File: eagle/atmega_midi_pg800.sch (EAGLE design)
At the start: 19 parts, among them IC1 78L05Z, U1 6N138, U2 ATMEGA328P_PDIP, X1 MAB6H

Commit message: routed
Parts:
- removed MIDI_IN1: MIDIJACK, adafruit:MIDIJACK
- removed RESET2: LSP11, solpad:LSP11
- added C4: 100uF, rcl:CPOL-USB45181A
- added C5: 10uF, rcl:CPOL-USB45181A
- added MIDI_THRU: MIDIJACK, adafruit:MIDIJACK
- added X2: 22-23-2081, con-molex:22-23-2081
- RESET: value LSP11 -> 22-23-2021; device solpad:LSP11 -> con-molex:22-23-2021
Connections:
- new net N$10: U2.PB2(SS/OC1B), X1.1
- new net N$11: U2.PB1(OC1A), X1.5
- new net N$12: U2.PC0(ADC0), X2-7.S
- new net N$13: U2.PC1(ADC1), X2-6.S
- new net N$14: U2.PC2(ADC2), X2-5.S
- new net N$15: U2.PC3(ADC3), X2-4.S
- new net N$16: U2.PC4(ADC4/SDA), X2-3.S
- new net N$17: U2.PC5(ADC5/SCL), X2-2.S
- new net N$2: D2.A, X1.3
- new net N$6: C4.+, D2.C, IC1.VI
- new net N$9: U2.PB0(ICP), X1.6
- net +5V: now also C5.+, IC1.VO, X2-1.S
- net GND: now also C4.-, C5.-, IC1.GND, MIDI_THRUG$1.2, MIDI_THRUG$2.MT, MIDI_THRUG$3.MT, MIDI_THRUG$4.MT, MIDI_THRUG$5.MT, RESET-1.S, X1.4, X1.PE, X2-8.S; no longer MIDI_IN1G$1.2, MIDI_IN1G$2.MT, MIDI_IN1G$3.MT, MIDI_IN1G$4.MT, MIDI_IN1G$5.MT, RESET2.MP
- net N$1: now also MIDI_THRUG$1.4; no longer MIDI_IN1G$1.4
- net N$42: now also MIDI_THRUG$1.5; no longer MIDI_IN1G$1.5
- net N$43: now also RESET-2.S; no longer RESET.MP
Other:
- moved on the sheet: D2, IC1, R3, R5

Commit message: gcode
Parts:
- Q1: value (none) -> 16.000Mhz
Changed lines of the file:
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@@
 <parts>
 <part name="U2" library="SparkFun-DigitalIC" deviceset="ATMEGA328P_PDIP" device=""/>
-<part name="Q1" library="crystal" deviceset="CRYSTAL" device="HC49S"/>
+<part name="Q1" library="crystal" deviceset="CRYSTAL" device="HC49S" value="16.000Mhz"/>
 <part name="C1" library="rcl" deviceset="C-US" device="025-040X050" value="27pF"/>
 <part name="C2" library="rcl" deviceset="C-US" device="025-040X050" value="27pF"/>
@@
 <instance part="C4" gate="G$1" x="91.44" y="53.34"/>
 <instance part="C5" gate="G$1" x="60.96" y="53.34"/>
-<instance part="P+4" gate="1" x="60.96" y="73.66"/>
+<instance part="P+4" gate="1" x="60.96" y="66.04"/>
 <instance part="GND4" gate="1" x="60.96" y="43.18"/>
 <instance part="GND5" gate="1" x="91.44" y="43.18"/>
@@
 <wire x1="60.96" y1="60.96" x2="60.96" y2="55.88" width="0.1524" layer="91"/>
 <pinref part="P+4" gate="1" pin="+5V"/>
-<wire x1="60.96" y1="71.12" x2="60.96" y2="60.96" width="0.1524" layer="91"/>
+<wire x1="60.96" y1="63.5" x2="60.96" y2="60.96" width="0.1524" layer="91"/>
 <junction x="60.96" y="60.96"/>
 </segment>

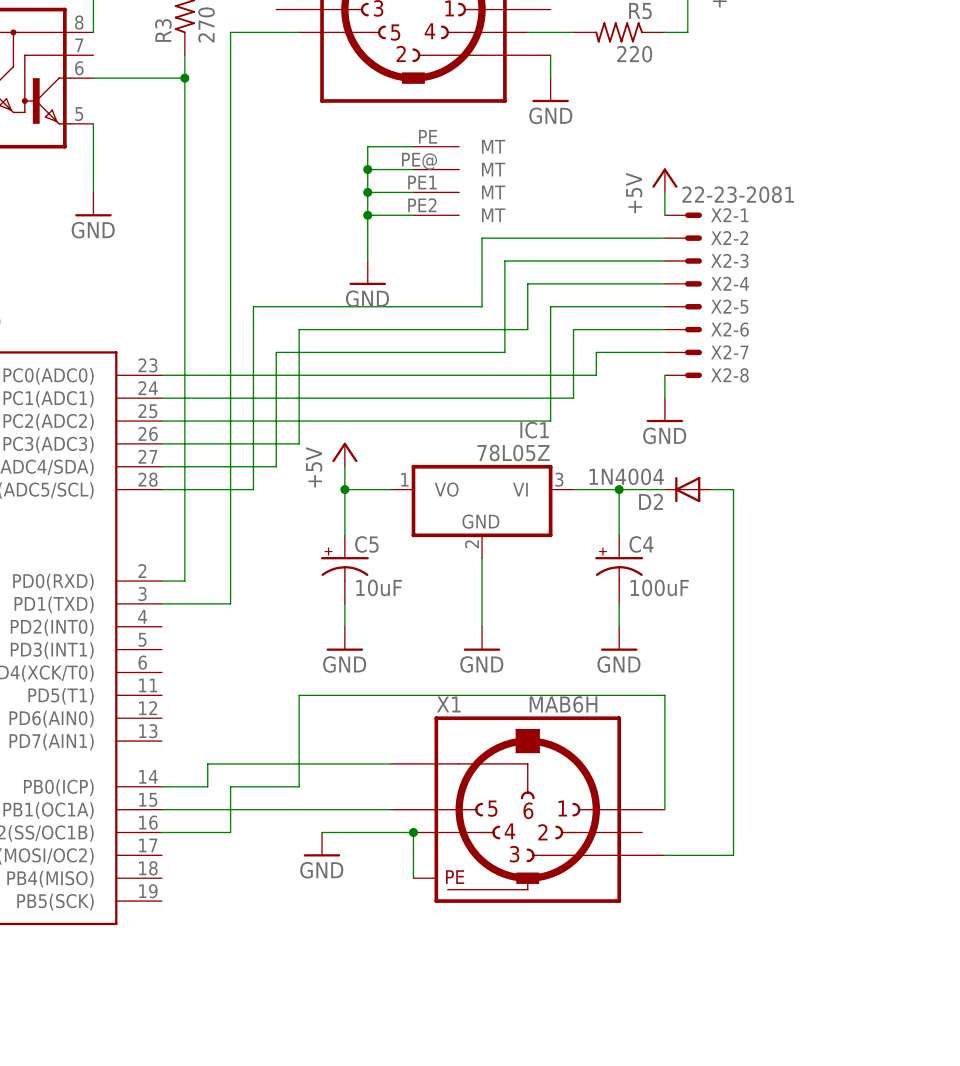
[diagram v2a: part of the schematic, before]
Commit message: added oled disply connection
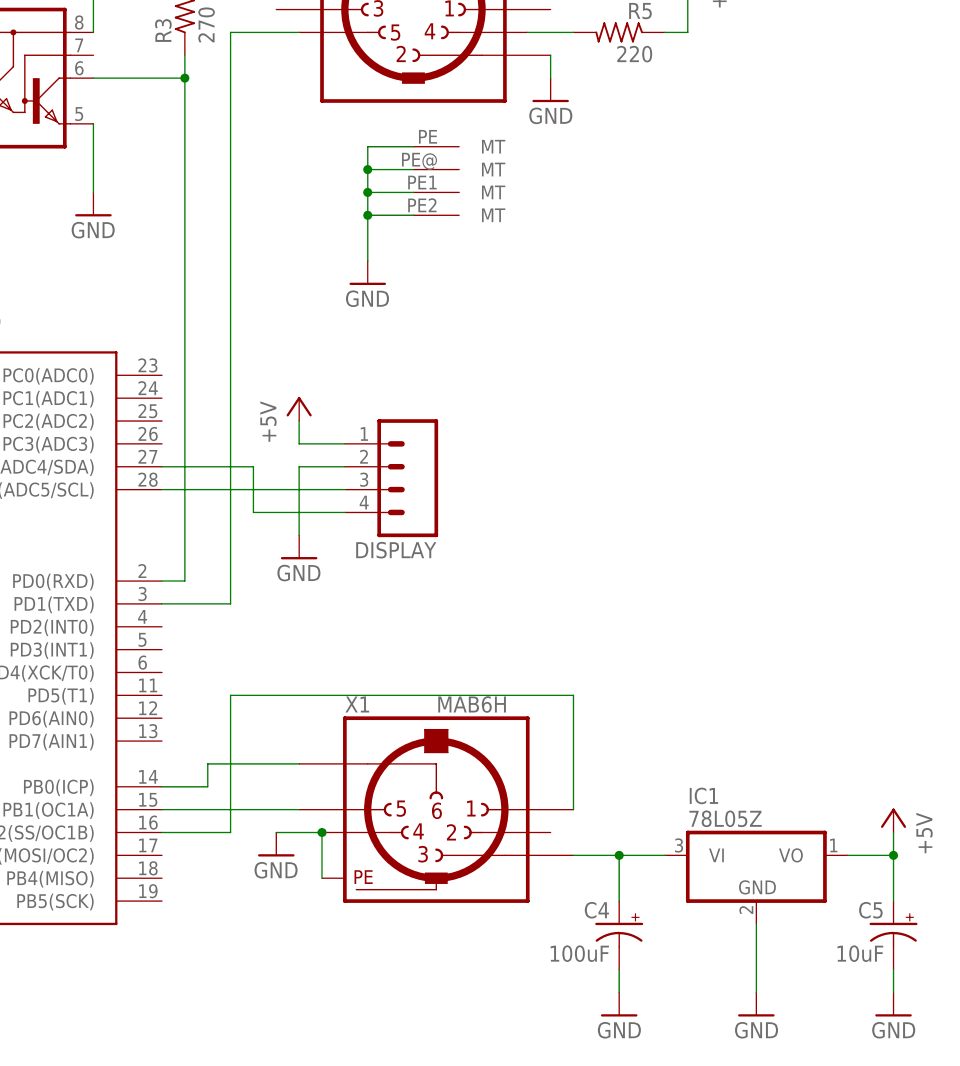
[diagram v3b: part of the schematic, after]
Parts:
- removed D2: 1N4004, adafruit:1N4004
- removed X2: 22-23-2081, con-molex:22-23-2081
- added DISPLAY: (no value), SparkFun-Connectors:M04POLAR
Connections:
- removed net N$14: U2.PC2(ADC2), X2-5.S
- removed net N$15: U2.PC3(ADC3), X2-4.S
- removed net N$16: U2.PC4(ADC4/SDA), X2-3.S
- removed net N$17: U2.PC5(ADC5/SCL), X2-2.S
- removed net N$2: D2.A, X1.3
- net +5V: now also DISPLAY.1; no longer X2-1.S
- net GND: now also DISPLAY.2; no longer X2-8.S
- net N$12: now also DISPLAY.3, U2.PC5(ADC5/SCL); no longer U2.PC0(ADC0), X2-7.S
- net N$13: now also DISPLAY.4, U2.PC4(ADC4/SDA); no longer U2.PC1(ADC1), X2-6.S
- net N$6: now also X1.3; no longer D2.C
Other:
- moved on the sheet: C4, C5, IC1, X1

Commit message: mux coming in
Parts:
- added IC2, IC3, IC4: 4067N, 40xx:4067N
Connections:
- new net N$14: IC3A.X, U2.PC1(ADC1)
- new net N$15: IC2A.X, U2.PC2(ADC2)
- new net N$2: IC4A.X, U2.PC0(ADC0)
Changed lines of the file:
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@@
 <part name="P+5" library="supply1" deviceset="+5V" device=""/>
 <part name="GND7" library="supply1" deviceset="GND" device=""/>
+<part name="IC2" library="40xx" deviceset="4067" device="N"/>
+<part name="IC3" library="40xx" deviceset="4067" device="N"/>
+<part name="IC4" library="40xx" deviceset="4067" device="N"/>
 </parts>
 <sheets>
@@
 <instance part="P+5" gate="1" x="55.88" y="71.12"/>
 <instance part="GND7" gate="1" x="55.88" y="53.34"/>
+<instance part="IC2" gate="A" x="106.68" y="60.96"/>
+<instance part="IC3" gate="A" x="139.7" y="60.96"/>
+<instance part="IC4" gate="A" x="172.72" y="60.96"/>
 </instances>
 <busses>
@@
 </segment>
 </net>
+<net name="N$2" class="0">
+<segment>
+<wire x1="86.36" y1="99.06" x2="86.36" y2="73.66" width="0.1524" layer="91"/>
+<pinref part="U2" gate="G$1" pin="PC0(ADC0)"/>
+<wire x1="86.36" y1="73.66" x2="40.64" y2="73.66" width="0.1524" layer="91"/>
+<pinref part="IC4" gate="A" pin="X"/>
+<wire x1="86.36" y1="99.06" x2="185.42" y2="99.06" width="0.1524" layer="91"/>
+<wire x1="185.42" y1="99.06" x2="185.42" y2="71.12" width="0.1524" layer="91"/>
+</segment>
+</net>
+<net name="N$14" class="0">
+<segment>
+<pinref part="IC3" gate="A" pin="X"/>
+<wire x1="152.4" y1="71.12" x2="152.4" y2="96.52" width="0.1524" layer="91"/>
+<wire x1="152.4" y1="96.52" x2="88.9" y2="96.52" width="0.1524" layer="91"/>
+<wire x1="88.9" y1="96.52" x2="88.9" y2="71.12" width="0.1524" layer="91"/>
+<pinref part="U2" gate="G$1" pin="PC1(ADC1)"/>
+<wire x1="88.9" y1="71.12" x2="40.64" y2="71.12" width="0.1524" layer="91"/>
+</segment>
+</net>
+<net name="N$15" class="0">
+<segment>
+<pinref part="U2" gate="G$1" pin="PC2(ADC2)"/>
+<wire x1="40.64" y1="68.58" x2="91.44" y2="68.58" width="0.1524" layer="91"/>
+<wire x1="91.44" y1="68.58" x2="91.44" y2="93.98" width="0.1524" layer="91"/>
+<pinref part="IC2" gate="A" pin="X"/>
+<wire x1="91.44" y1="93.98" x2="119.38" y2="93.98" width="0.1524" layer="91"/>
+<wire x1="119.38" y1="93.98" x2="119.38" y2="71.12" width="0.1524" layer="91"/>
+</segment>
+</net>

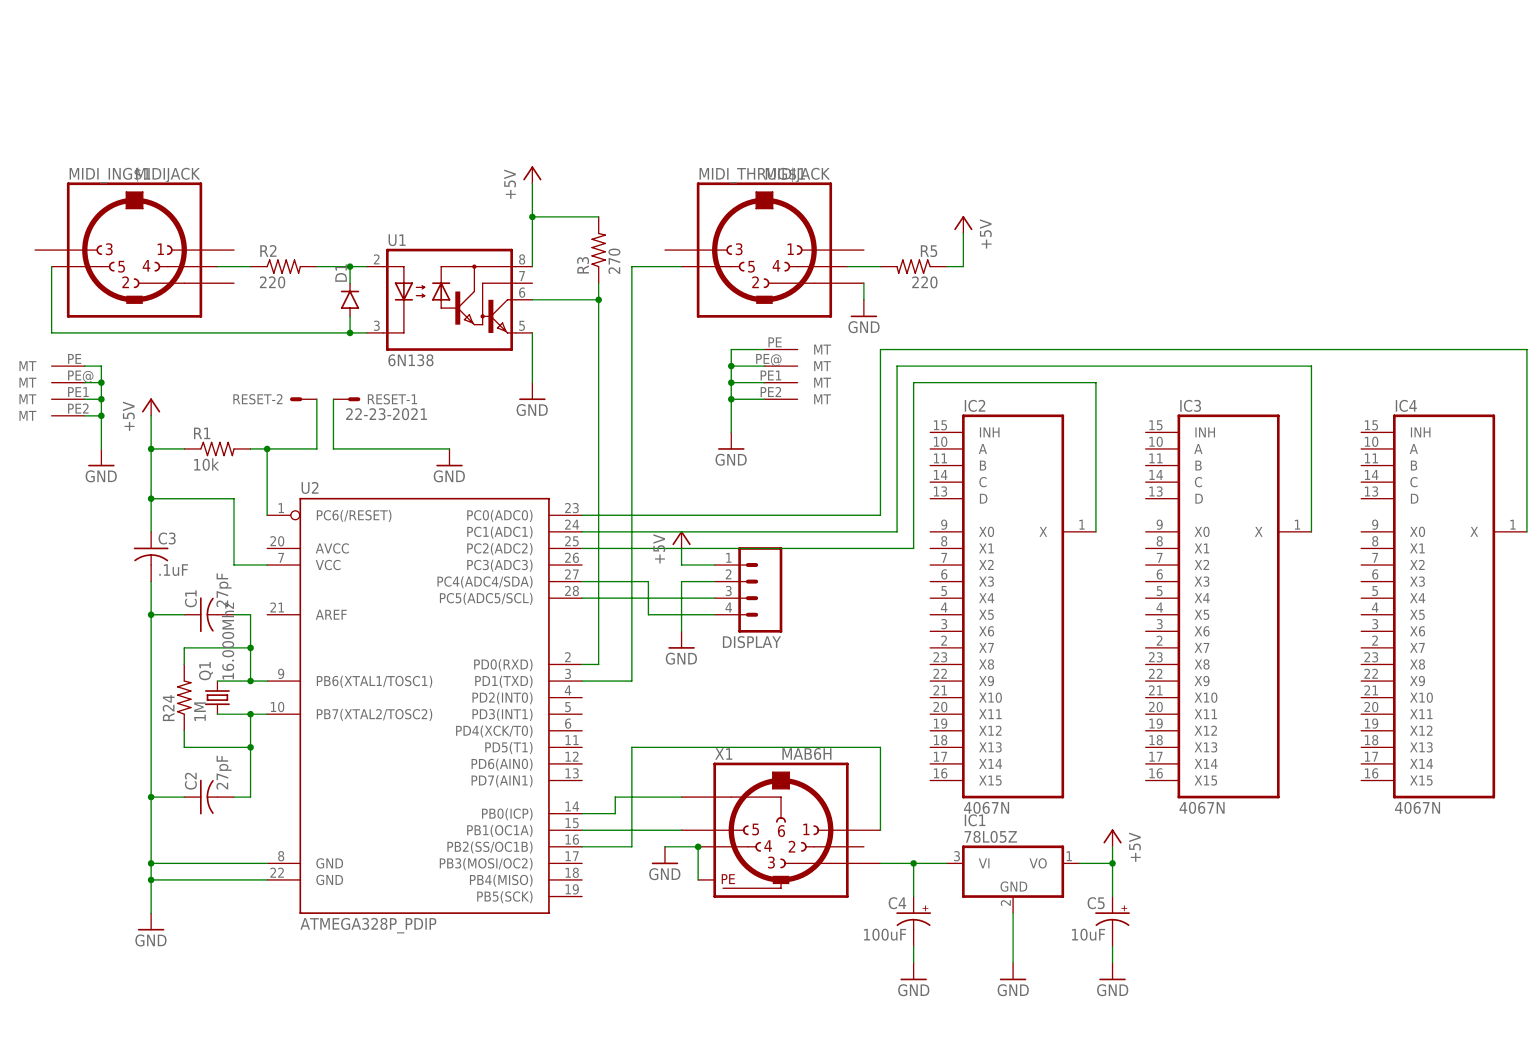
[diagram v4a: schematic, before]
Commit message: muxes with input holes
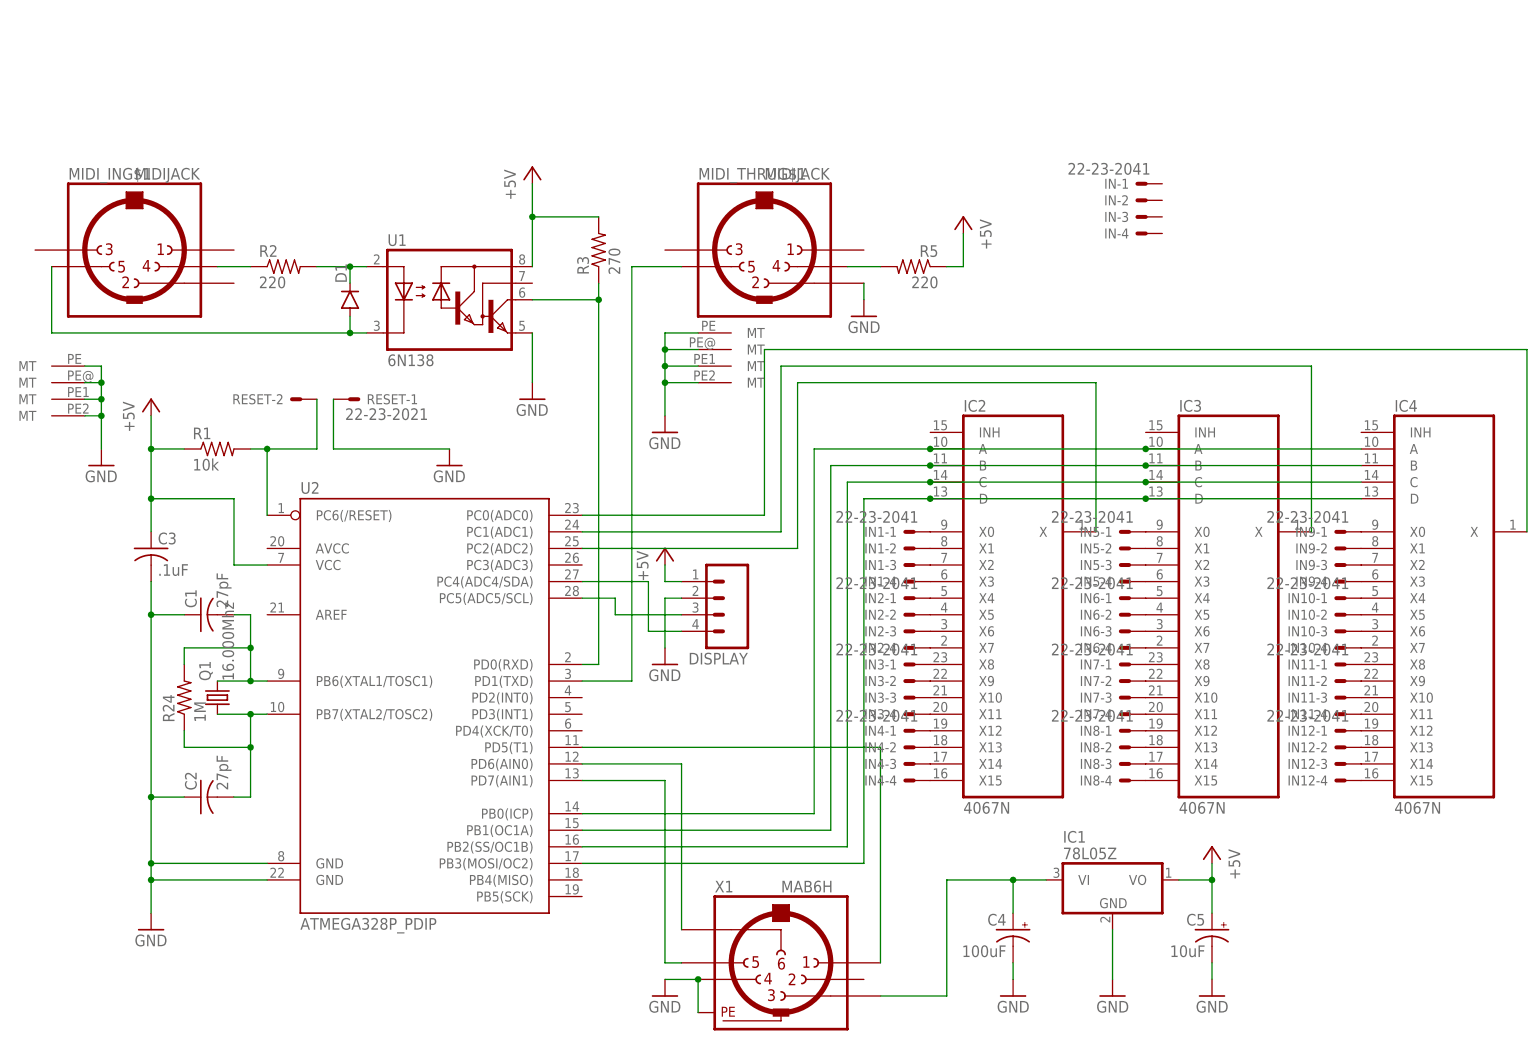
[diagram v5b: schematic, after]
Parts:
- added IN, IN1, IN10, IN11, IN12, IN2, IN3, IN4, IN5, IN6, IN7, IN8, IN9: 22-23-2041, con-molex:22-23-2041
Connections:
- new net N$16: IC2A.A, IC3A.A, IC4A.A, U2.PB0(ICP)
- new net N$17: IC2A.B, IC3A.B, IC4A.B, U2.PB1(OC1A)
- new net N$18: IC2A.C, IC3A.C, IC4A.C, U2.PB2(SS/OC1B)
- new net N$19: IC2A.D, IC3A.D, IC4A.D, U2.PB3(MOSI/OC2)
- net N$10: now also U2.PD5(T1); no longer U2.PB2(SS/OC1B)
- net N$11: now also U2.PD7(AIN1); no longer U2.PB1(OC1A)
- net N$9: now also U2.PD6(AIN0); no longer U2.PB0(ICP)
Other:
- moved on the sheet: C4, C5, DISPLAY, IC1, X1

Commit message: input terminals wired
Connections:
- new net N$20: IC2A.X0, IN1-1.S
- new net N$21: IC2A.X1, IN1-2.S
- new net N$22: IC2A.X2, IN1-3.S
- new net N$23: IC2A.X3, IN1-4.S
- new net N$24: IC2A.X4, IN2-1.S
- new net N$25: IC2A.X5, IN2-2.S
- new net N$26: IC2A.X6, IN2-3.S
- new net N$27: IC2A.X7, IN2-4.S
- new net N$28: IC2A.X8, IN3-1.S
- new net N$29: IC2A.X9, IN3-2.S
- new net N$31: IC2A.X10, IN3-3.S
- new net N$32: IC2A.X11, IN3-4.S
- new net N$33: IC2A.X12, IN4-1.S
- new net N$34: IC2A.X13, IN4-2.S
- new net N$35: IC2A.X14, IN4-3.S
- new net N$36: IC2A.X15, IN4-4.S
- new net N$37: IC3A.X0, IN5-1.S
- new net N$38: IC3A.X1, IN5-2.S
- new net N$39: IC3A.X2, IN5-3.S
- new net N$40: IC3A.X3, IN5-4.S
- new net N$41: IC3A.X4, IN6-1.S
- new net N$44: IC3A.X5, IN6-2.S
- new net N$45: IC3A.X6, IN6-3.S
- new net N$46: IC3A.X7, IN6-4.S
- new net N$47: IC3A.X8, IN7-1.S
- new net N$48: IC3A.X9, IN7-2.S
- new net N$49: IC3A.X10, IN7-3.S
- new net N$50: IC3A.X11, IN7-4.S
- new net N$51: IC3A.X12, IN8-1.S
- new net N$52: IC3A.X13, IN8-2.S
- new net N$53: IC3A.X14, IN8-3.S
- new net N$54: IC3A.X15, IN8-4.S
- new net N$55: IC4A.X0, IN9-1.S
- new net N$56: IC4A.X1, IN9-2.S
- new net N$57: IC4A.X2, IN9-3.S
- new net N$58: IC4A.X3, IN9-4.S
- new net N$59: IC4A.X4, IN10-1.S
- new net N$60: IC4A.X5, IN10-2.S
- new net N$61: IC4A.X6, IN10-3.S
- new net N$62: IC4A.X7, IN10-4.S
- new net N$63: IC4A.X8, IN11-1.S
- new net N$64: IC4A.X9, IN11-2.S
- new net N$65: IC4A.X10, IN11-3.S
- new net N$66: IC4A.X11, IN11-4.S
- new net N$67: IC4A.X12, IN12-1.S
- new net N$68: IC4A.X13, IN12-2.S
- new net N$69: IC4A.X14, IN12-3.S
- new net N$70: IC4A.X15, IN12-4.S
